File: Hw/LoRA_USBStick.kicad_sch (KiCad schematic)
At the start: 37 parts

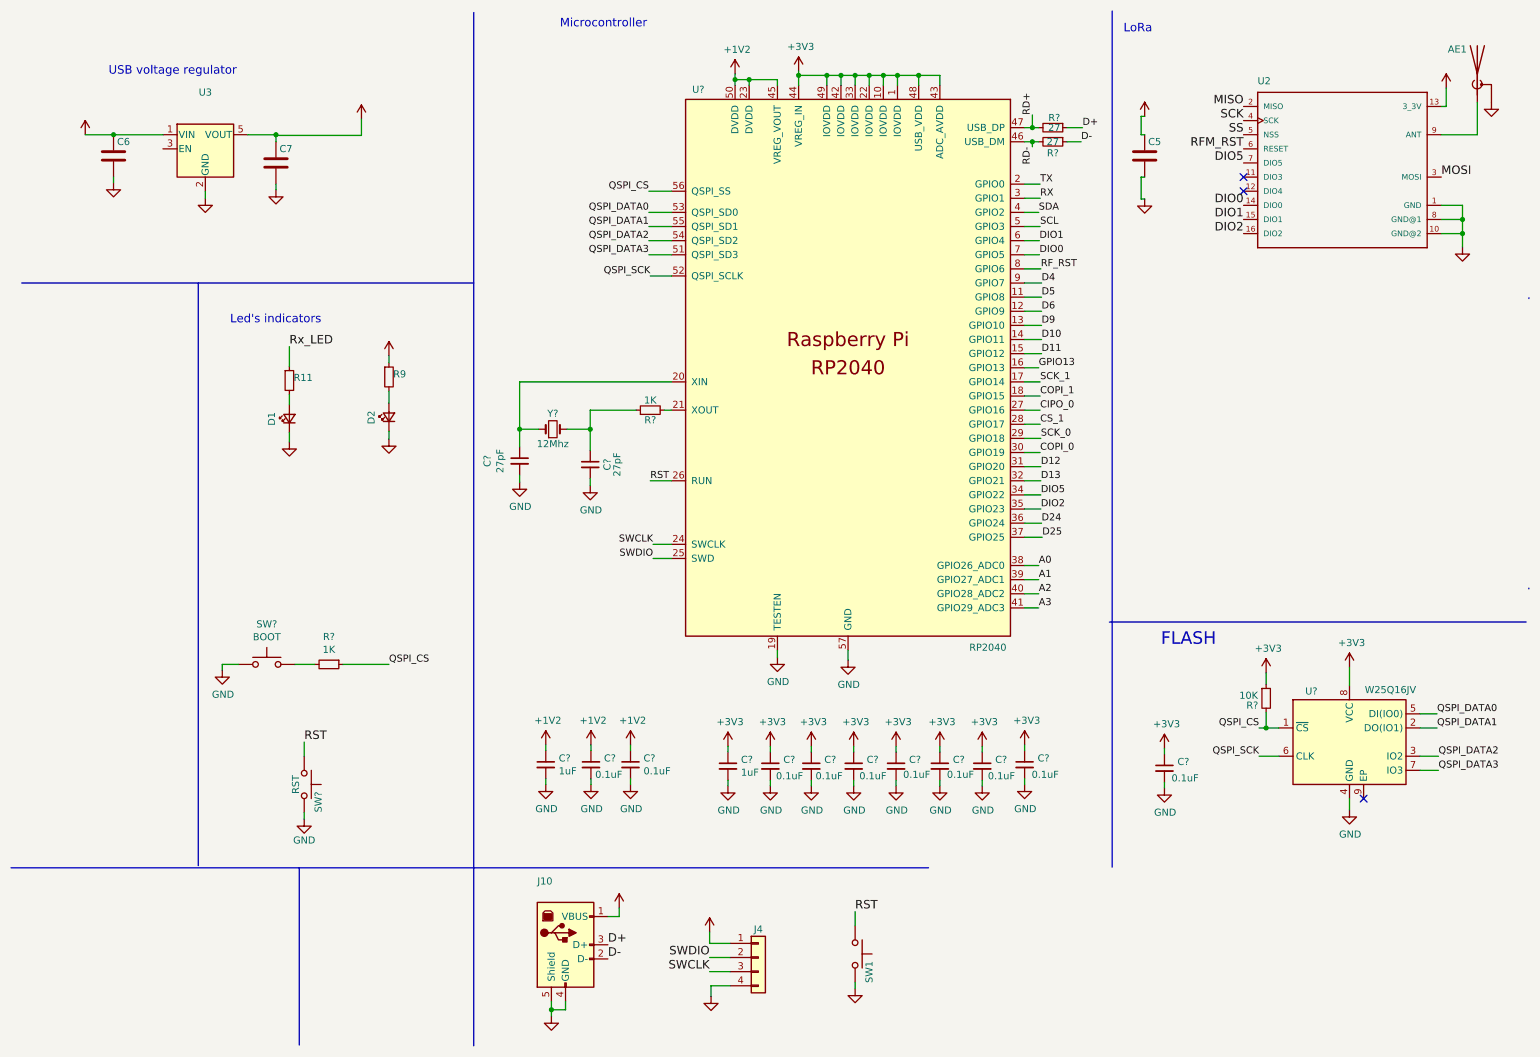
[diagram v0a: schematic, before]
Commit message: Assigned footprints
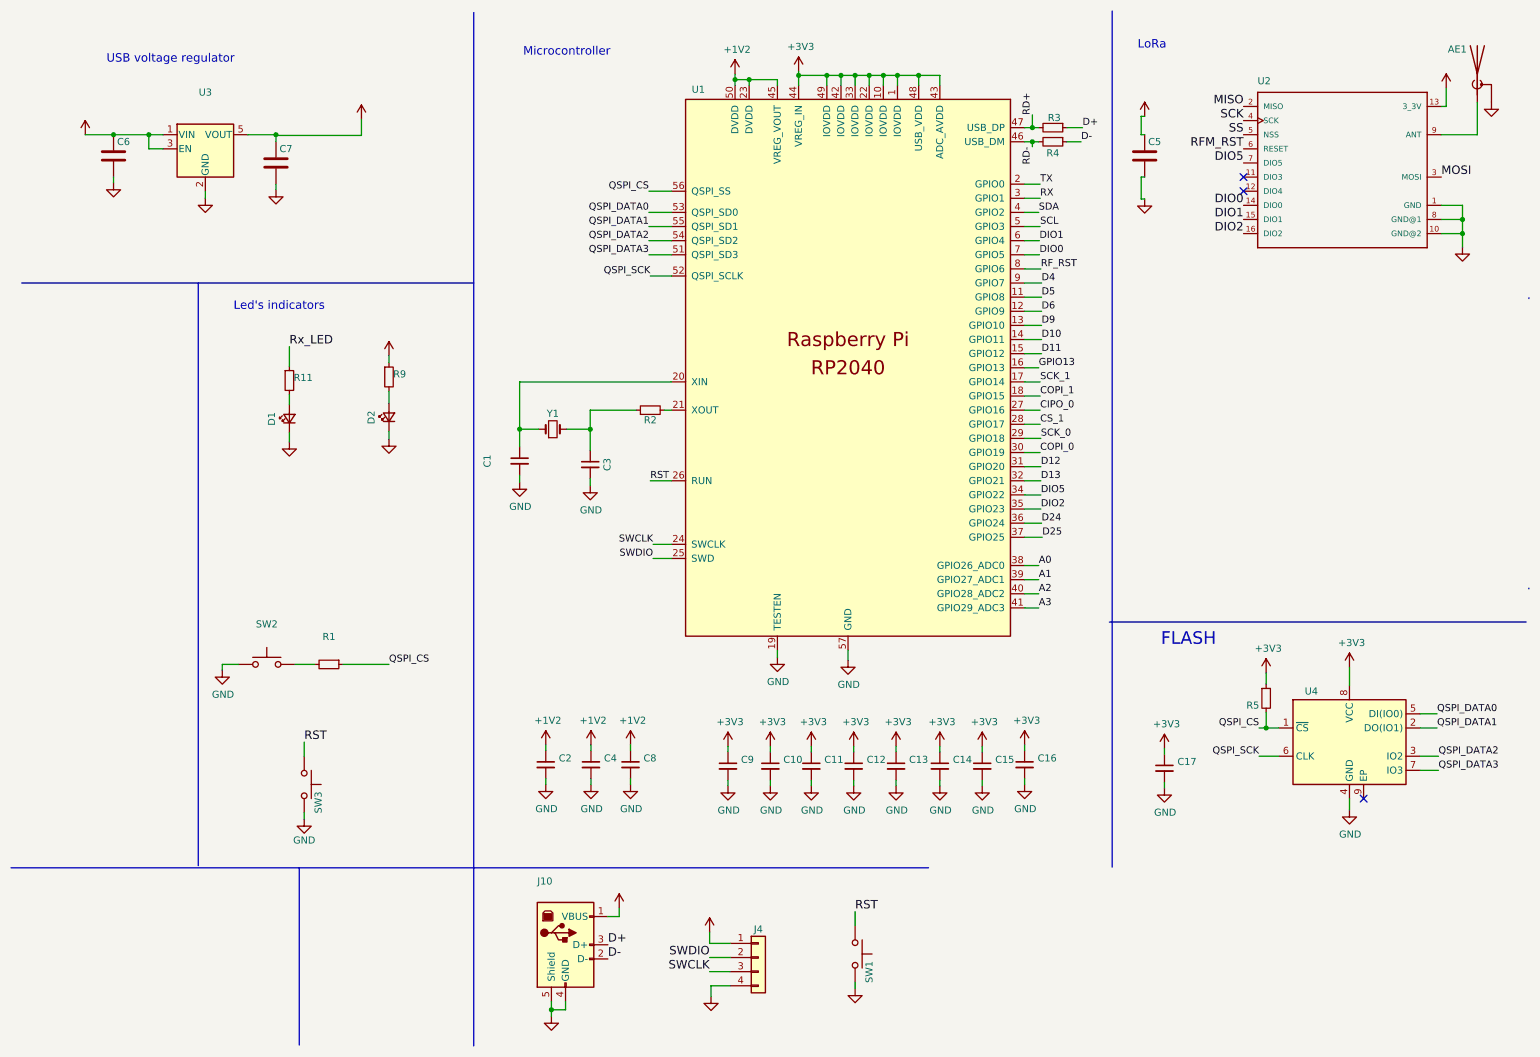
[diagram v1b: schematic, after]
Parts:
- C1, C3: renamed from C?; value 27pF -> (none); footprint Capacitor_SMD:C_0603_1608Metric -> (none)
- C10, C11, C12, C13, C14, C15, C16, C17, C4, C8: renamed from C?; value 0.1uF -> (none); footprint Capacitor_SMD:C_0603_1608Metric -> (none)
- C2, C9: renamed from C?; value 1uF -> (none); footprint Capacitor_SMD:C_0603_1608Metric -> (none)
- R1, R2: renamed from R?; value 1K -> (none); footprint Resistor_SMD:R_0603_1608Metric -> (none)
- R3, R4: renamed from R?; value 27 -> (none); footprint Resistor_SMD:R_0603_1608Metric -> (none)
- R5: renamed from R?; value 10K -> (none); footprint Resistor_SMD:R_0603_1608Metric -> (none)
- SW2: renamed from SW?; value BOOT -> (none); footprint Button_Switch_SMD:SW_SPST_TL3342 -> (none)
- SW3: renamed from SW?; value RST -> (none); footprint Button_Switch_SMD:SW_SPST_TL3342 -> (none)
- U1: renamed from U?; value RP2040 -> (none); footprint badge_pwnCon:RP2040-QFN-56 -> (none)
- U4: renamed from U?; value W25Q16JV -> (none); footprint Package_SO:SOIC-8_5.275x5.275mm_P1.27mm -> (none)
- Y1: renamed from Y?; value 12Mhz -> (none); footprint Crystal:Crystal_SMD_HC49-SD -> (none); manf# ABLS-12.000MHZ-B4-T -> ECS-120-18-30-JGN-TR
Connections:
- net VBUS: now also U3.3 (EN)

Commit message: Change labels, assigned and check the footprints
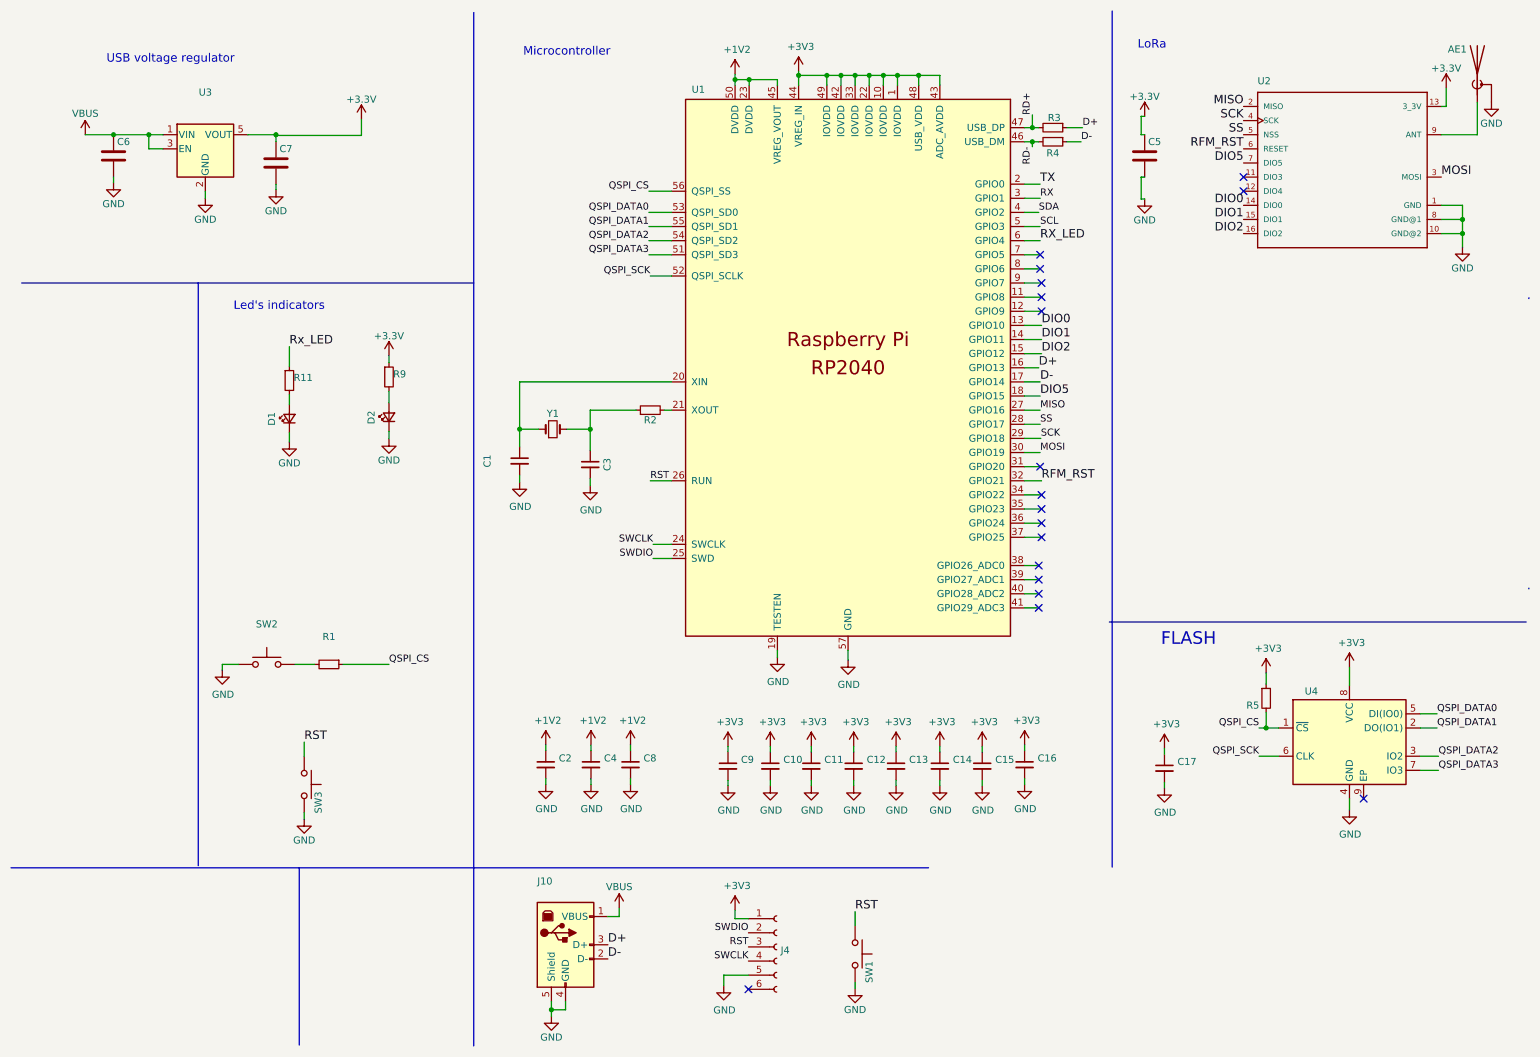
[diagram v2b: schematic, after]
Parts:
- removed J4: (no value), symbol LoRA_USBStick-rescue:Conn_01x04
- added J4: (no value), symbol Connector:Conn_01x06_Female
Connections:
- net CIPO_0 is gone; now on net MISO: U1.27 (GPIO16)
- net COPI_0 is gone; now on net MOSI: U1.30 (GPIO19)
- net COPI_1 is gone; now on net DIO5: U1.18 (GPIO15)
- net CS_1 is gone; now on net SS: U1.28 (GPIO17)
- net D10 is gone; now on net DIO1: U1.14 (GPIO11)
- net D11 is gone; now on net DIO2: U1.15 (GPIO12)
- net D13 is gone; now on net RFM_RST: U1.32 (GPIO21)
- net D9 is gone; now on net DIO0: U1.13 (GPIO10)
- net GPIO13 is gone; now on net D+: U1.16 (GPIO13)
- net SCK_0 is gone; now on net SCK: U1.29 (GPIO18)
- net SCK_1 is gone; now on net D-: U1.17 (GPIO14)
- net +3V3: now also J4.1 (Pin_1)
- net DIO0: no longer U1.7 (GPIO5)
- net DIO1: no longer U1.6 (GPIO4)
- net DIO2: no longer U1.35 (GPIO23)
- net DIO5: no longer U1.34 (GPIO22)
- net GND: now also J4.5 (Pin_5)
- net RST: now also J4.3 (Pin_3)
- net SWCLK: now also J4.4 (Pin_4)
- net SWDIO: now also J4.2 (Pin_2)
- net A0: no longer names the net of U1.38 (GPIO26_ADC0)
- net A1: no longer names the net of U1.39 (GPIO27_ADC1)
- net A2: no longer names the net of U1.40 (GPIO28_ADC2)
- net A3: no longer names the net of U1.41 (GPIO29_ADC3)
- net D12: no longer names the net of U1.31 (GPIO20)
- net D24: no longer names the net of U1.36 (GPIO24)
- net D25: no longer names the net of U1.37 (GPIO25)
- net D4: no longer names the net of U1.9 (GPIO7)
- net D5: no longer names the net of U1.11 (GPIO8)
- net D6: no longer names the net of U1.12 (GPIO9)
- net RF_RST: no longer names the net of U1.8 (GPIO6)
- new net RX_LED: U1.6 (GPIO4)
- no-connect marks 3 -> 18

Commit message: change labels for memory and RX_LED
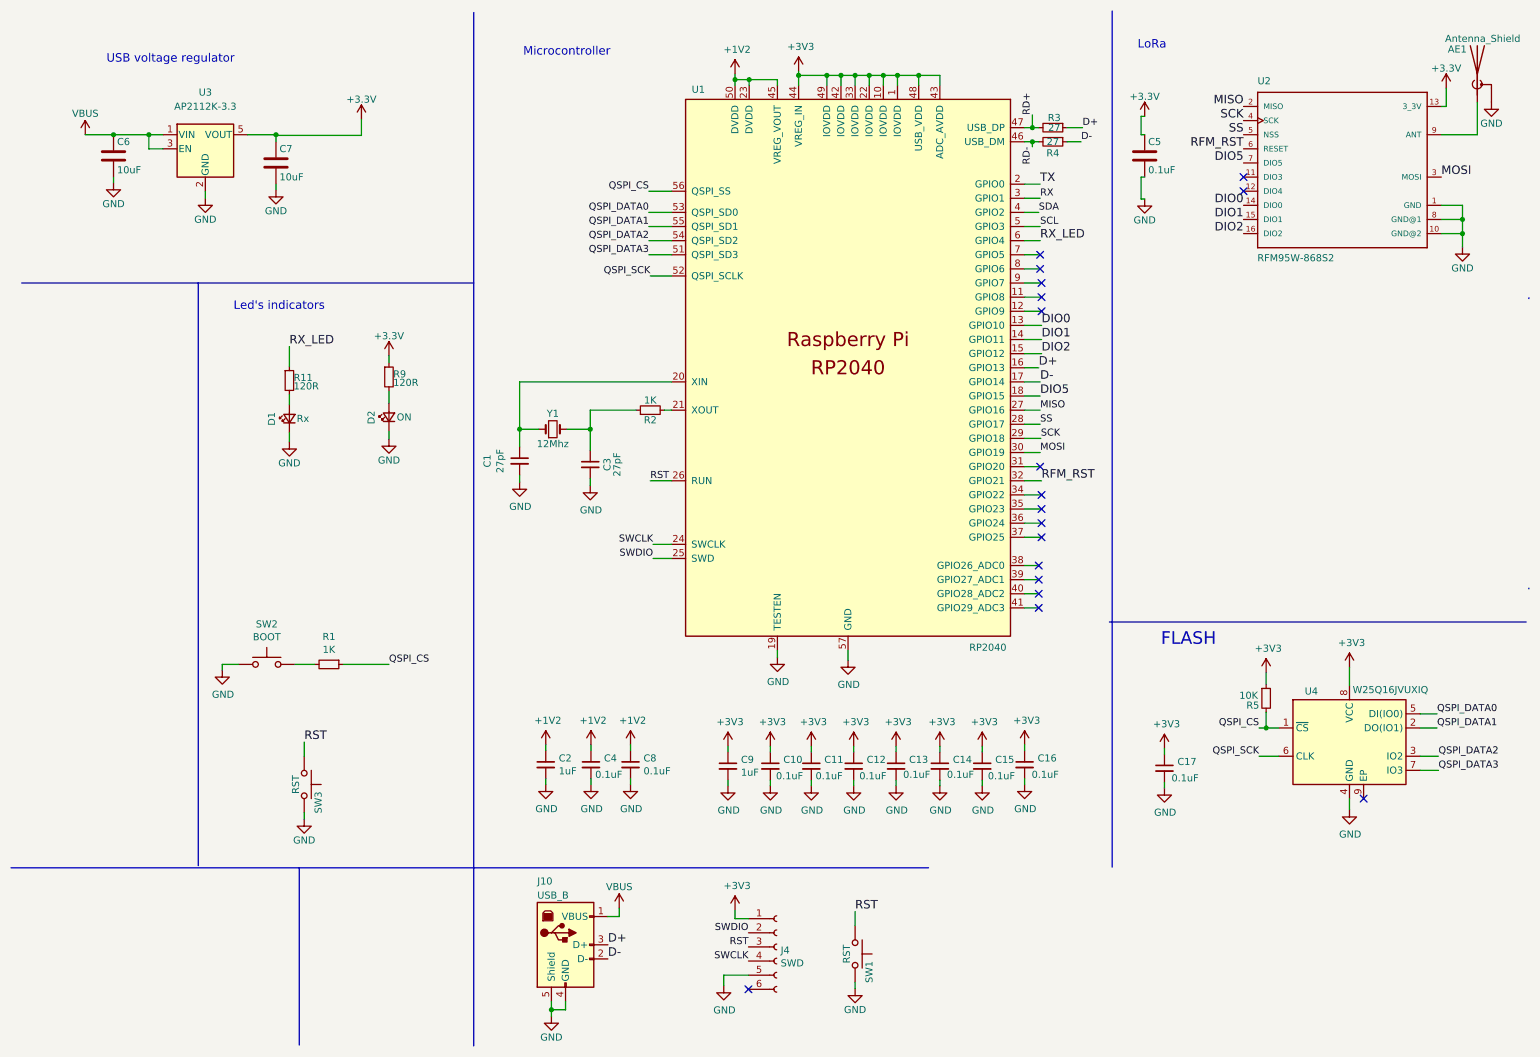
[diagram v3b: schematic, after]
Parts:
- AE1: value (none) -> Antenna_Shield; footprint (none) -> agroin:SMA_EDGE
- C1, C3: value (none) -> 27pF; footprint (none) -> Capacitor_SMD:C_0603_1608Metric
- C10, C11, C12, C13, C14, C15, C16, C17, C4, C8: value (none) -> 0.1uF; footprint (none) -> Capacitor_SMD:C_0603_1608Metric
- C2, C9: value (none) -> 1uF; footprint (none) -> Capacitor_SMD:C_0603_1608Metric
- C5: value (none) -> 0.1uF; footprint (none) -> Capacitor_SMD:C_0805_2012Metric_Pad1.15x1.40mm_HandSolder
- C6, C7: value (none) -> 10uF; footprint (none) -> Capacitor_SMD:C_0805_2012Metric_Pad1.15x1.40mm_HandSolder
- D1: value (none) -> Rx; footprint (none) -> LED_SMD:LED_0805_2012Metric_Pad1.15x1.40mm_HandSolder
- D2: value (none) -> ON; footprint (none) -> LED_SMD:LED_0805_2012Metric_Pad1.15x1.40mm_HandSolder
- J10: value (none) -> USB_B; footprint (none) -> Connectors:C46394
- J4: value (none) -> SWD; footprint (none) -> Connector:Tag-Connect_TC2030-IDC-NL_2x03_P1.27mm_Vertical
- R1, R2: value (none) -> 1K; footprint (none) -> Resistor_SMD:R_0603_1608Metric
- R11, R9: value (none) -> 120R; footprint (none) -> Resistor_SMD:R_0805_2012Metric_Pad1.15x1.40mm_HandSolder
- R3, R4: value (none) -> 27; footprint (none) -> Resistor_SMD:R_0603_1608Metric
- R5: value (none) -> 10K; footprint (none) -> Resistor_SMD:R_0603_1608Metric
- SW1, SW3: value (none) -> RST; footprint (none) -> Button_Switch_SMD:SW_SPST_TL3342
- SW2: value (none) -> BOOT; footprint (none) -> Button_Switch_SMD:SW_SPST_TL3342
- U1: value (none) -> RP2040; footprint (none) -> RP2040:RP2040-QFN-56
- U2: value (none) -> RFM95W-868S2; footprint (none) -> RF_Module:HOPERF_RFM9XW_SMD
- U3: value (none) -> AP2112K-3.3; footprint (none) -> Package_TO_SOT_SMD:SOT-23-5
- U4: value (none) -> W25Q16JVUXIQ; footprint (none) -> Package_SO:SOIC-8_5.275x5.275mm_P1.27mm
- Y1: value (none) -> 12Mhz; footprint (none) -> Crystal:Crystal_SMD_5032-2Pin_5.0x3.2mm
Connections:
- net Rx_LED is gone; now on net RX_LED: R11.1
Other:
- title: USB Stick -> USB Stick RP2040

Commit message: remove duplicate tags, I2C and UART
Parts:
- U4: value W25Q16JVUXIQ -> W25Q16JV
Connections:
- net TX is gone; now on net RX_LED: U1.2 (GPIO0)
- net D+: no longer U1.16 (GPIO13)
- net D-: no longer U1.17 (GPIO14)
- net RX_LED: no longer R11.1, U1.6 (GPIO4)
- net RX: no longer names the net of U1.3 (GPIO1)
- net SCL: no longer names the net of U1.5 (GPIO3)
- net SDA: no longer names the net of U1.4 (GPIO2)
- new net Rx_LED: R11.1
- no-connect marks 18 -> 24
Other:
- title: USB Stick RP2040 -> USB Stick
